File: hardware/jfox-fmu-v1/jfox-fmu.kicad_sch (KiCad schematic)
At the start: 0 parts

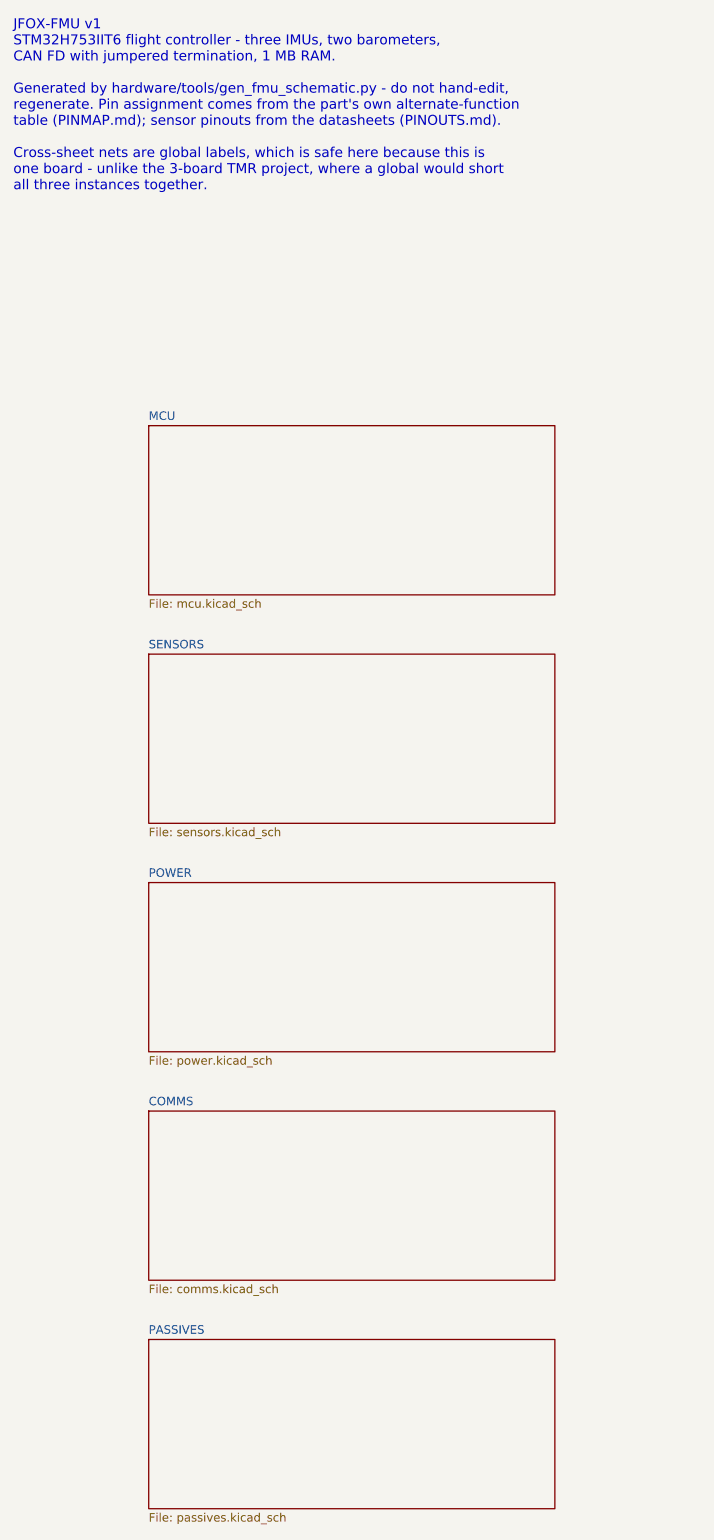
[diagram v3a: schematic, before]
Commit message: Connectors, and three more wires that went nowhere
Eleven headers on a new sheet, Pixhawk pinouts on JST-GH 1.25 mm: two TELEM,
two GPS, RC, a 10-way debug, external SPI, both power inputs, safety switch,
and the eight PWM channels. Pixhawk's pinout rather than a novel one because
the ecosystem's GPS units, radios and power modules are built to it, and a
different pinout means a custom loom for every peripheral.

Isolated nets 48 -> 10.

Three more defects found on the way, all the same shape as the last batch -
something that looked wired and was not:

  C20 decoupled a net called "VDDA" that nothing else joined. The MCU's VDDA
  pin is on +3V3A. The analog rail's bypass capacitor was connected to
  nothing at all.

  LED_R/G/B had MCU pins allocated and drove nothing - the board had no way
  to say anything. Now three LEDs with series resistors, common anode.

  And the two_pin helper assumed every two-pin part is drawn vertically. It
  splits the pins on dy < 0, but Device:LED is horizontal with both pins at
  dy = 0, so both took the same net: D1 shorted its own anode to its cathode
  while the anode net kept only the series resistor. It looked wired and was
  a short. Now split on whichever axis actually separates the pins.

The debug header went from 6 ways to 10. Six could carry SWD and USART1_TX
but not RX, so the console would have been write-only.

Worth recording: when the passives sheet outgrew A4 mid-change, the generator
correctly refused to write - and every checker then passed against the
PREVIOUS generation still on disk. Green on stale files. The fix was to
re-lay-out and regenerate before trusting any of it, but the trap is real and
worth knowing about.

Remaining 10 isolated nets are honest and all blocked on the same two things:
UV1-3_SET and OV1-3_SET need the LTC4417's threshold equations, PGATE1-3 need
its external PMOS pass devices, and both need the datasheet, which would not
download in this session. SD_DETECT needs a socket symbol that ex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
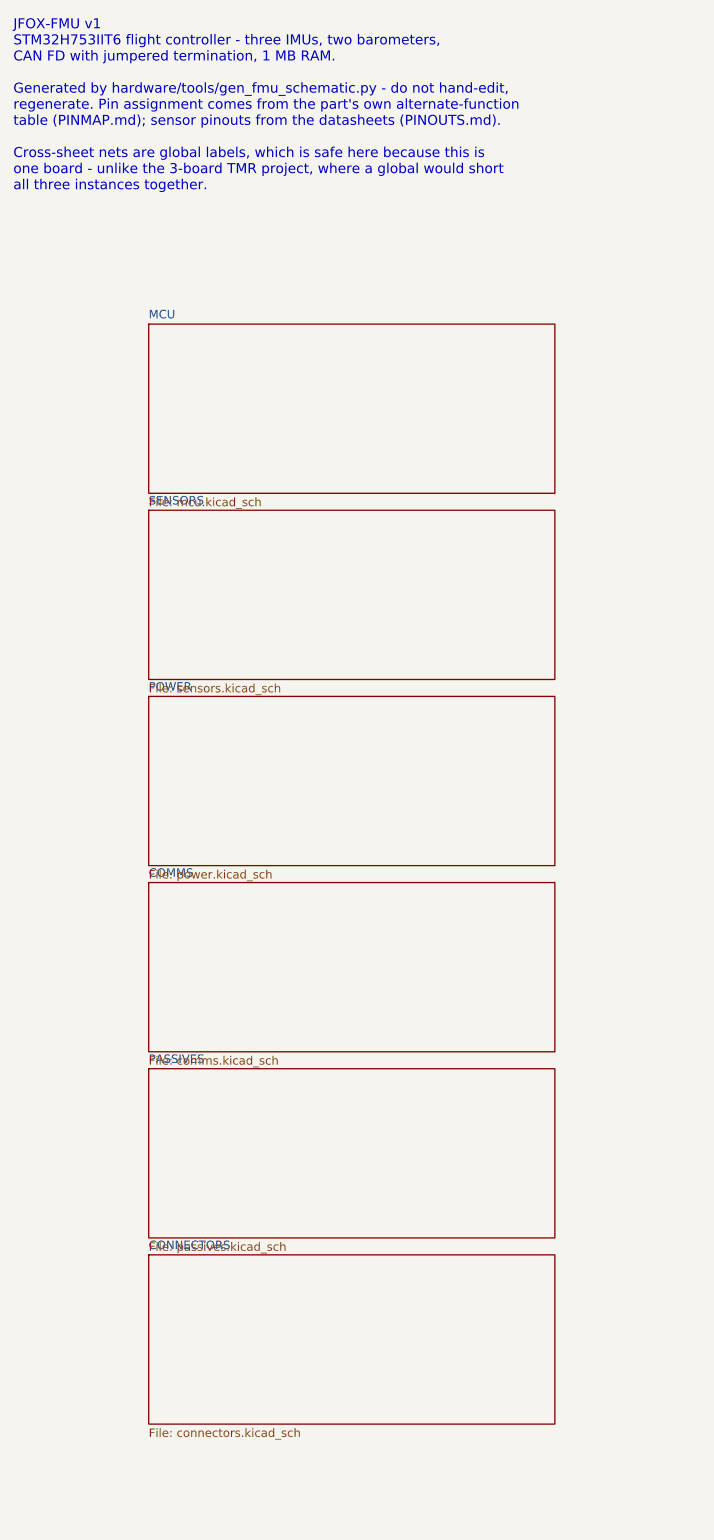
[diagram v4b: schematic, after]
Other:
- added sheet CONNECTORS (connectors.kicad_sch)
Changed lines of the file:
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@@
 		(comment 1 "STM32H753IIT6 - 3 IMUs, 2 barometers, magnetometer, CAN FD")
 		(comment 2 "Generated by hardware/tools/gen_fmu_schematic.py - regenerate, do not edit")
-		(comment 3 "Sheet 1 of 6")
+		(comment 3 "Sheet 1 of 7")
 	)
 	(text "JFOX-FMU v1\nSTM32H753IIT6 flight controller - three IMUs, two barometers,\nCAN FD with jumpered termination, 1 MB RAM.\n\nGenerated by hardware/tools/gen_fmu_schematic.py - do not hand-edit,\nregenerate. Pin assignment comes from the part's own alternate-function\ntable (PINMAP.md); sensor pinouts from the datasheets (PINOUTS.md).\n\nCross-sheet nets are global labels, which is safe here because this is\none board - unlike the 3-board TMR project, where a global would short\nall three instances together."
@@
 	)
 	(sheet
-		(at 115.57 74.93)
+		(at 115.57 59.69)
 		(size 60.96 25.4)
 		(fields_autoplaced yes)
@@
 		(fill (color 0 0 0 0.0000))
 		(property "Sheetname" "MCU"
-			(at 115.57 74.22 0)
+			(at 115.57 58.98 0)
 			(effects (font (size 1.27 1.27))(justify left bottom))
 		)
 		(property "Sheetfile" "mcu.kicad_sch"
-			(at 115.57 100.93 0)
+			(at 115.57 85.69 0)
 			(effects (font (size 1.27 1.27))(justify left top))
 		)
 		(instances
 			(project "jfox-fmu"
-				(path "/b1bdd5c4-7c42-4129-99eb-566d358cf911"
+				(path "/63e8cca2-7ac2-491b-b7d8-b6d628731540"
 					(page "2")
 				)
@@
 	)
 	(sheet
-		(at 115.57 109.22)
+		(at 115.57 87.63)
 		(size 60.96 25.4)
 		(fields_autoplaced yes)
@@
 		(fill (color 0 0 0 0.0000))
 		(property "Sheetname" "SENSORS"
-			(at 115.57 108.51 0)
+			(at 115.57 86.92 0)
 			(effects (font (size 1.27 1.27))(justify left bottom))
 		)
 		(property "Sheetfile" "sensors.kicad_sch"
-			(at 115.57 135.22 0)
+			(at 115.57 113.63 0)
 			(effects (font (size 1.27 1.27))(justify left top))
 		)
 		(instances
 			(project "jfox-fmu"
-				(path "/b1bdd5c4-7c42-4129-99eb-566d358cf911"
+				(path "/63e8cca2-7ac2-491b-b7d8-b6d628731540"
 					(page "3")
+				)
+			)
+		)
+	)
+	(sheet
+		(at 115.57 115.57)
+		(size 60.96 25.4)
+		(fields_autoplaced yes)
+		(stroke (width 0.1524)(type solid))
+		(fill (color 0 0 0 0.0000))
+		(property "Sheetname" "POWER"
+			(at 115.57 114.86 0)
+			(effects (font (size 1.27 1.27))(justify left bottom))
+		)
+		(property "Sheetfile" "power.kicad_sch"
+			(at 115.57 141.57 0)
+			(effects (font (size 1.27 1.27))(justify left top))
+		)
+		(instances
+			(project "jfox-fmu"
+				(path "/63e8cca2-7ac2-491b-b7d8-b6d628731540"
+					(page "4")
 				)
 			)
@@
 		(stroke (width 0.1524)(type solid))
 		(fill (color 0 0 0 0.0000))
-		(property "Sheetname" "POWER"
+		(property "Sheetname" "COMMS"
 			(at 115.57 142.8 0)
 			(effects (font (size 1.27 1.27))(justify left bottom))
 		)
-		(property "Sheetfile" "power.kicad_sch"
+		(property "Sheetfile" "comms.kicad_sch"
 			(at 115.57 169.51 0)
 			(effects (font (size 1.27 1.27))(justify left top))
@@
 		(instances
 			(project "jfox-fmu"
-				(path "/b1bdd5c4-7c42-4129-99eb-566d358cf911"
-					(page "4")
-				)
-			)
-		)
-	)
-	(sheet
-		(at 115.57 177.8)
-		(size 60.96 25.4)
-		(fields_autoplaced yes)
-		(stroke (width 0.1524)(type solid))
-		(fill (color 0 0 0 0.0000))
-		(property "Sheetname" "COMMS"
-			(at 115.57 177.09 0)
-			(effects (font (size 1.27 1.27))(justify left bottom))
-		)
-		(property "Sheetfile" "comms.kicad_sch"
-			(at 115.57 203.8 0)
-			(effects (font (size 1.27 1.27))(justify left top))
-		)
-		(instances
-			(project "jfox-fmu"
-				(path "/b1bdd5c4-7c42-4129-99eb-566d358cf911"
+				(path "/63e8cca2-7ac2-491b-b7d8-b6d628731540"
 					(page "5")
 				)
@@
 	)
 	(sheet
-		(at 115.57 212.09)
+		(at 115.57 171.45)
 		(size 60.96 25.4)
 		(fields_autoplaced yes)
@@
 		(fill (color 0 0 0 0.0000))
 		(property "Sheetname" "PASSIVES"
-			(at 115.57 211.38 0)
+			(at 115.57 170.74 0)
 			(effects (font (size 1.27 1.27))(justify left bottom))
 		)
 		(property "Sheetfile" "passives.kicad_sch"
-			(at 115.57 238.09 0)
+			(at 115.57 197.45 0)
 			(effects (font (size 1.27 1.27))(justify left top))
 		)
 		(instances
 			(project "jfox-fmu"
-				(path "/b1bdd5c4-7c42-4129-99eb-566d358cf911"
+				(path "/63e8cca2-7ac2-491b-b7d8-b6d628731540"
 					(page "6")
 				)
 			)
+		)
+	)
+	(sheet
+		(at 115.57 199.39)
+		(size 60.96 25.4)
+		(fields_autoplaced yes)
+		(stroke (width 0.1524)(type solid))
+		(fill (color 0 0 0 0.0000))
+		(property "Sheetname" "CONNECTORS"
+			(at 115.57 198.68 0)
+			(effects (font (size 1.27 1.27))(justify left bottom))
+		)
+		(property "Sheetfile" "connectors.kicad_sch"
+			(at 115.57 225.39 0)
+			(effects (font (size 1.27 1.27))(justify left top))
+		)
+		(instances
+			(project "jfox-fmu"
+				(path "/63e8cca2-7ac2-491b-b7d8-b6d628731540"
+					(page "7")
+				)
+			)

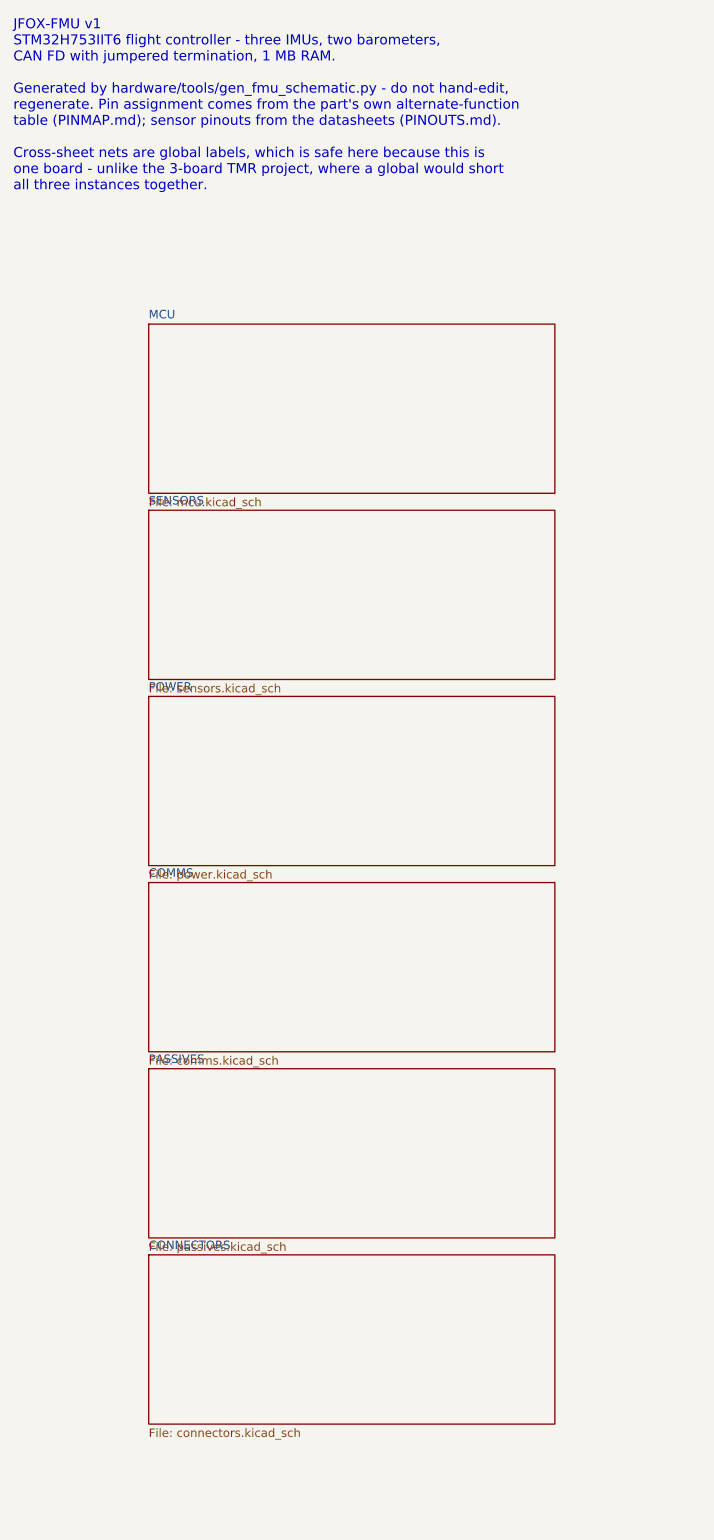
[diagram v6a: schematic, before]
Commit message: EMI/EMC protection, and the stackup that actually decides it
Full review first: schematic, footprints, sheet fit and traceability all pass;
objective passes 12 of 13 with fibre the only gap; environmental passes the
category and reports its known gaps. ERC 89, of which 75 are deliberately
unallocated GPIO.

A new protection sheet closes HWR-ENV-006 and HWR-ENV-007, and adds the
emissions control that DO-160G s21 would otherwise fail on. This board carries
two deliberate switching sources - U21 at 2.5 MHz and each ISOW1044's internal
converter at 25 MHz - and every off-board harness is an antenna bonded to
them.

  D4/D5/D6  6 V TVS on brick, servo and USB inputs. Above the 5.5 V a valid
            supply reaches, below what the LTC4417 and the buck tolerate.
            Unidirectional - reverse battery is the LTC4417's job.
  U40       USBLC6-2SC6 between J30 and the choke, closest to the connector
            so it protects the choke too, not only the MCU.
  L5        common-mode choke on USB, after the ESD array.
  L3/L4     common-mode chokes on both CAN pairs, with D7/D8 across them.
  FB1-3     ferrites on the 5 V feed to the telemetry, GPS and RC harnesses,
            because conducted emissions leave on the power wire as readily as
            on the signal wires.

The CAN protection references GND_ISO, not GND. Referencing it to board ground
would bridge the isolation barrier and undo the reason the ISOW1044 is there.

PCB_STACKUP_AND_EMC.md carries the half of EMC that is not a component:

**Six layers, not four.** A 4-layer SIG/GND/PWR/SIG leaves the inner power
layer split - and this board splits it four ways for the switched sensor rails
plus the analog and isolated domains. A signal crossing a split has no return
beneath it, so the return detours and the loop it encloses is the radiating
element. Six layers puts solid ground either side of the power layer, so every
signal has an unbroken return whatever the power layer is doing. That is the
single mos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
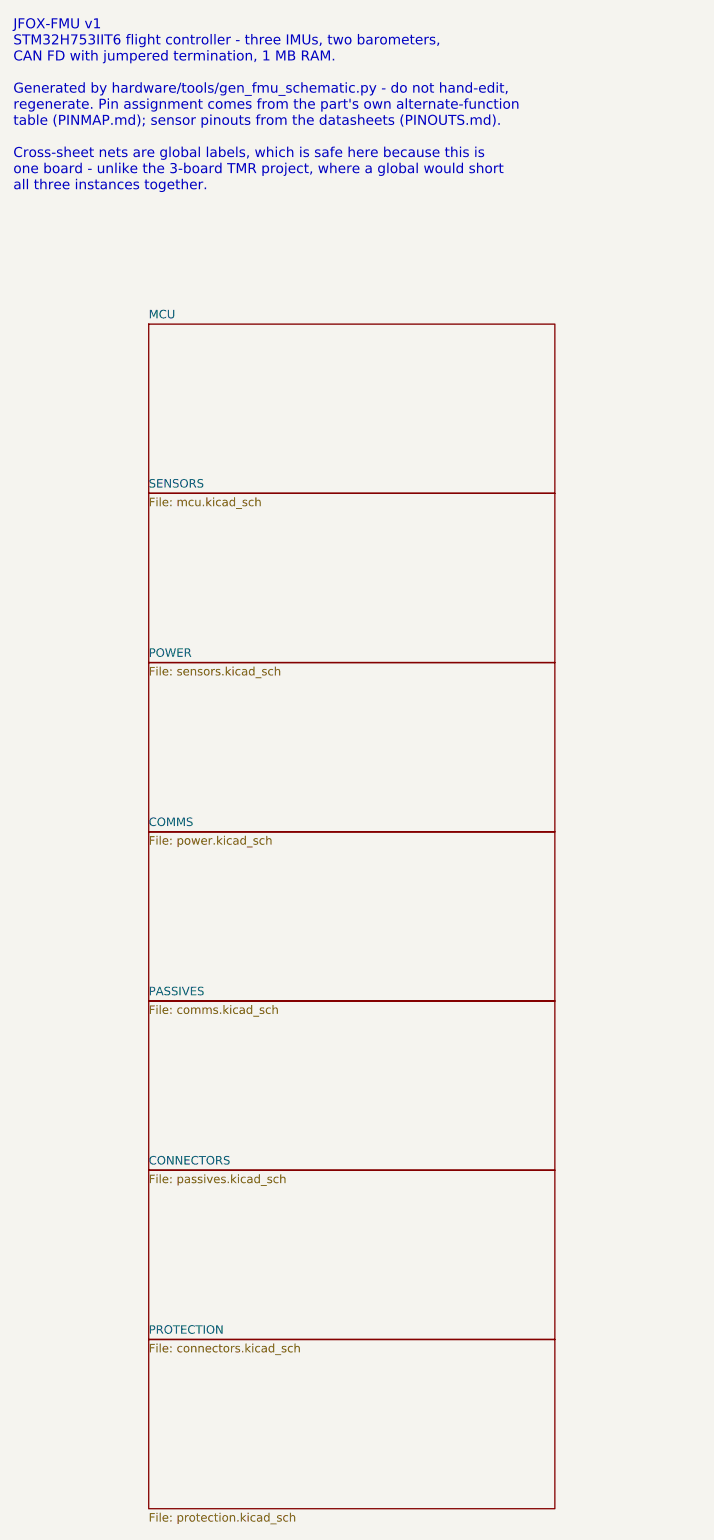
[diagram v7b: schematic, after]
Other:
- added sheet PROTECTION (protection.kicad_sch)
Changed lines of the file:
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@@
 		(comment 1 "STM32H753IIT6 - 3 IMUs, 2 barometers, magnetometer, CAN FD")
 		(comment 2 "Generated by hardware/tools/gen_fmu_schematic.py - regenerate, do not edit")
-		(comment 3 "Sheet 1 of 7")
+		(comment 3 "Sheet 1 of 8")
 	)
 	(text "JFOX-FMU v1\nSTM32H753IIT6 flight controller - three IMUs, two barometers,\nCAN FD with jumpered termination, 1 MB RAM.\n\nGenerated by hardware/tools/gen_fmu_schematic.py - do not hand-edit,\nregenerate. Pin assignment comes from the part's own alternate-function\ntable (PINMAP.md); sensor pinouts from the datasheets (PINOUTS.md).\n\nCross-sheet nets are global labels, which is safe here because this is\none board - unlike the 3-board TMR project, where a global would short\nall three instances together."
@@
 		(instances
 			(project "jfox-fmu"
-				(path "/4fcf8e0a-1f5d-4227-97a6-e228ea8df1ae"
+				(path "/fb92632d-e232-4770-9546-3bcc8564e3fc"
 					(page "2")
 				)
@@
 	)
 	(sheet
-		(at 115.57 87.63)
+		(at 115.57 85.09)
 		(size 60.96 25.4)
 		(fields_autoplaced yes)
@@
 		(fill (color 0 0 0 0.0000))
 		(property "Sheetname" "SENSORS"
-			(at 115.57 86.92 0)
+			(at 115.57 84.38 0)
 			(effects (font (size 1.27 1.27))(justify left bottom))
 		)
 		(property "Sheetfile" "sensors.kicad_sch"
-			(at 115.57 113.63 0)
+			(at 115.57 111.09 0)
 			(effects (font (size 1.27 1.27))(justify left top))
 		)
 		(instances
 			(project "jfox-fmu"
-				(path "/4fcf8e0a-1f5d-4227-97a6-e228ea8df1ae"
+				(path "/fb92632d-e232-4770-9546-3bcc8564e3fc"
 					(page "3")
 				)
@@
 	)
 	(sheet
-		(at 115.57 115.57)
+		(at 115.57 110.49)
 		(size 60.96 25.4)
 		(fields_autoplaced yes)
@@
 		(fill (color 0 0 0 0.0000))
 		(property "Sheetname" "POWER"
-			(at 115.57 114.86 0)
+			(at 115.57 109.78 0)
 			(effects (font (size 1.27 1.27))(justify left bottom))
 		)
 		(property "Sheetfile" "power.kicad_sch"
-			(at 115.57 141.57 0)
+			(at 115.57 136.49 0)
 			(effects (font (size 1.27 1.27))(justify left top))
 		)
 		(instances
 			(project "jfox-fmu"
-				(path "/4fcf8e0a-1f5d-4227-97a6-e228ea8df1ae"
+				(path "/fb92632d-e232-4770-9546-3bcc8564e3fc"
 					(page "4")
 				)
@@
 	)
 	(sheet
-		(at 115.57 143.51)
+		(at 115.57 135.89)
 		(size 60.96 25.4)
 		(fields_autoplaced yes)
@@
 		(fill (color 0 0 0 0.0000))
 		(property "Sheetname" "COMMS"
-			(at 115.57 142.8 0)
+			(at 115.57 135.18 0)
 			(effects (font (size 1.27 1.27))(justify left bottom))
 		)
 		(property "Sheetfile" "comms.kicad_sch"
-			(at 115.57 169.51 0)
+			(at 115.57 161.89 0)
 			(effects (font (size 1.27 1.27))(justify left top))
 		)
 		(instances
 			(project "jfox-fmu"
-				(path "/4fcf8e0a-1f5d-4227-97a6-e228ea8df1ae"
+				(path "/fb92632d-e232-4770-9546-3bcc8564e3fc"
 					(page "5")
 				)
@@
 	)
 	(sheet
-		(at 115.57 171.45)
+		(at 115.57 161.29)
 		(size 60.96 25.4)
 		(fields_autoplaced yes)
@@
 		(fill (color 0 0 0 0.0000))
 		(property "Sheetname" "PASSIVES"
-			(at 115.57 170.74 0)
+			(at 115.57 160.58 0)
 			(effects (font (size 1.27 1.27))(justify left bottom))
 		)
 		(property "Sheetfile" "passives.kicad_sch"
-			(at 115.57 197.45 0)
+			(at 115.57 187.29 0)
 			(effects (font (size 1.27 1.27))(justify left top))
 		)
 		(instances
 			(project "jfox-fmu"
-				(path "/4fcf8e0a-1f5d-4227-97a6-e228ea8df1ae"
+				(path "/fb92632d-e232-4770-9546-3bcc8564e3fc"
 					(page "6")
 				)
@@
 	)
 	(sheet
-		(at 115.57 199.39)
+		(at 115.57 186.69)
 		(size 60.96 25.4)
 		(fields_autoplaced yes)
@@
 		(fill (color 0 0 0 0.0000))
 		(property "Sheetname" "CONNECTORS"
-			(at 115.57 198.68 0)
+			(at 115.57 185.98 0)
 			(effects (font (size 1.27 1.27))(justify left bottom))
 		)
 		(property "Sheetfile" "connectors.kicad_sch"
-			(at 115.57 225.39 0)
+			(at 115.57 212.69 0)
 			(effects (font (size 1.27 1.27))(justify left top))
 		)
 		(instances
 			(project "jfox-fmu"
-				(path "/4fcf8e0a-1f5d-4227-97a6-e228ea8df1ae"
+				(path "/fb92632d-e232-4770-9546-3bcc8564e3fc"
 					(page "7")
 				)
 			)
+		)
+	)
+	(sheet
+		(at 115.57 212.09)
+		(size 60.96 25.4)
+		(fields_autoplaced yes)
+		(stroke (width 0.1524)(type solid))
+		(fill (color 0 0 0 0.0000))
+		(property "Sheetname" "PROTECTION"
+			(at 115.57 211.38 0)
+			(effects (font (size 1.27 1.27))(justify left bottom))
+		)
+		(property "Sheetfile" "protection.kicad_sch"
+			(at 115.57 238.09 0)
+			(effects (font (size 1.27 1.27))(justify left top))
+		)
+		(instances
+			(project "jfox-fmu"
+				(path "/fb92632d-e232-4770-9546-3bcc8564e3fc"
+					(page "8")
+				)
+			)
